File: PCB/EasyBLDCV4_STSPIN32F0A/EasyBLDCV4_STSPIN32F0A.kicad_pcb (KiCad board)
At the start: 4 copper layers, 31 x 40 mm, 58 parts, among them J1 10159560-A00221RLF, J2 STLINK-V3MINIE-EDGE, Q1 IAUC60N04S6N031HATMA1, Q2 IAUC60N04S6N031HATMA1, Q3 IAUC60N04S6N031HATMA1, U1 INA180A1IDBVR, U2 STSPIN32F0A

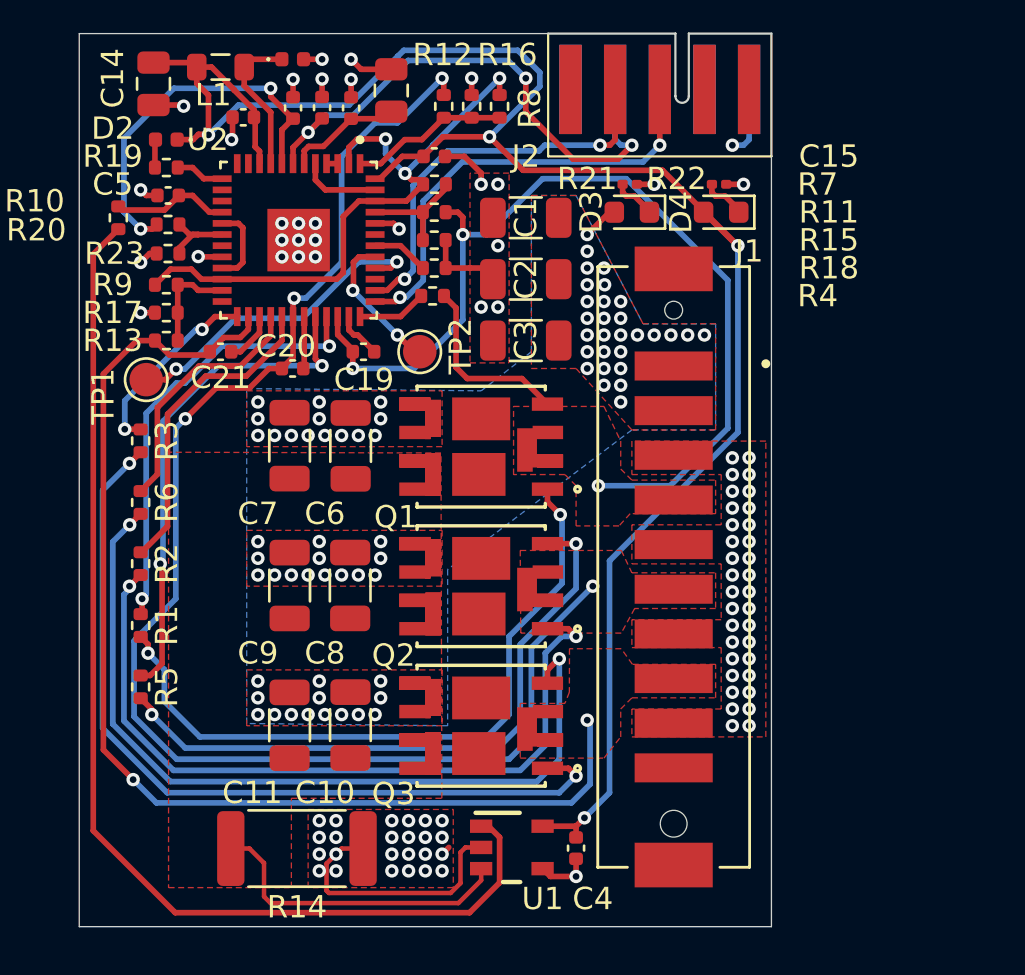
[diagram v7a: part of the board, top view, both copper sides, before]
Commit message: Changed out 0201 resistors, production version
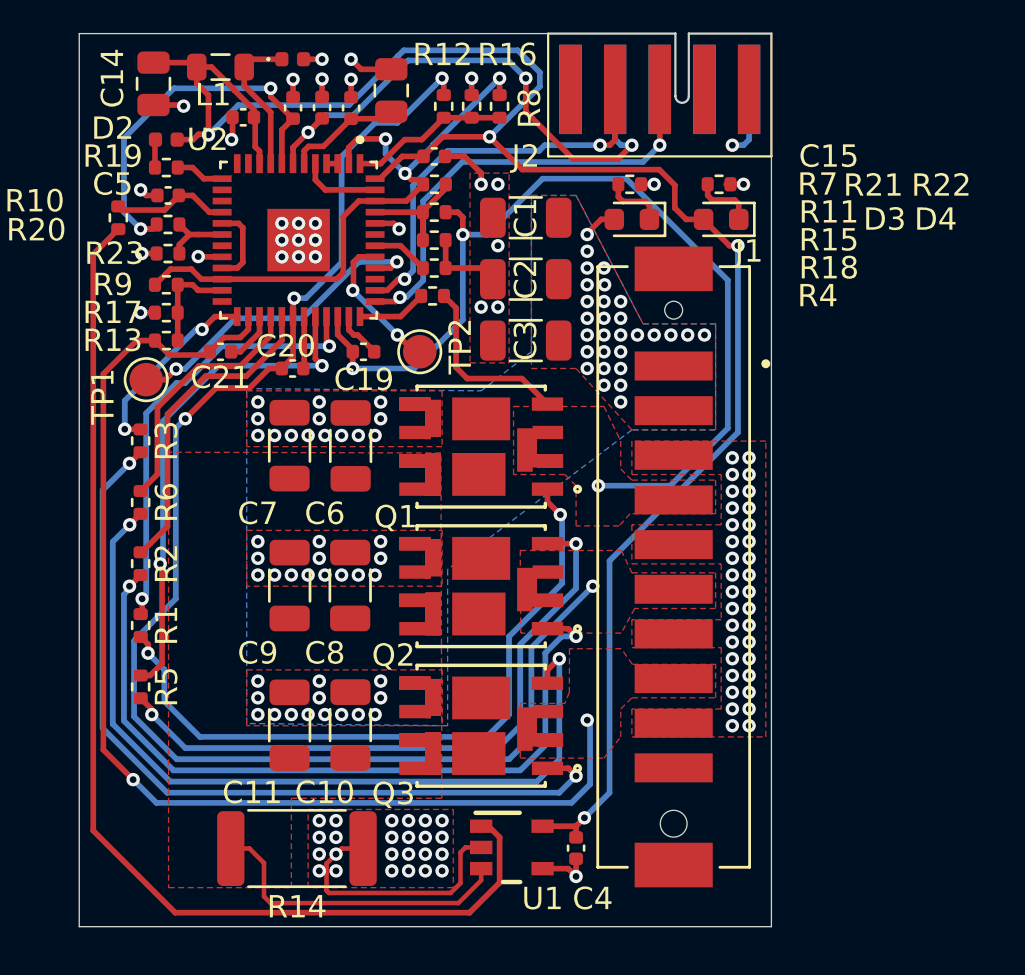
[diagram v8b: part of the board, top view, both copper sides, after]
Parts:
- C1, C10, C11, C2, C3, C6, C7, C8, C9: value 47u -> 22u
- D4: value GREEN -> RED
- R21, R22: footprint Resistor_SMD:R_0201_0603Metric -> Resistor_SMD:R_0402_1005Metric
- moved D3 0.32 mm to (163.2, 68.1)
- moved D4 0.32 mm to (167.2, 68.1)
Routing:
- net AVDD: track 85.8 -> 84.2 mm
- net GND: track 38.8 -> 38.2 mm
